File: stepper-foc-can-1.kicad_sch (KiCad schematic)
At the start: 0 parts

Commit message: schem: add stm32g474
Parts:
- added U1: STM32G474RBTx, Package_QFP:LQFP-64_10x10mm_P0.5mm, symbol MCU_ST_STM32G4:STM32G474RBTx
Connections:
- new net GND: U1.15 (VSS), U1.27 (VSSA), U1.31 (VSS), U1.47 (VSS), U1.63 (VSS)

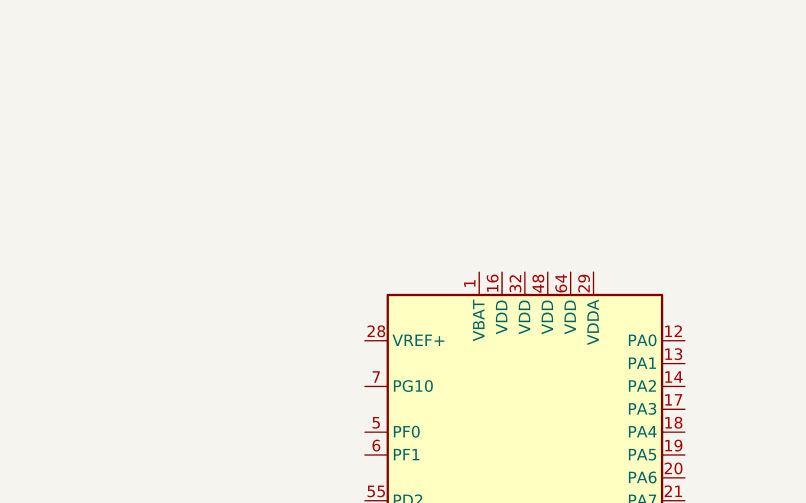
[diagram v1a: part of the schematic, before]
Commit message: schem: add stm32 decoupling caps
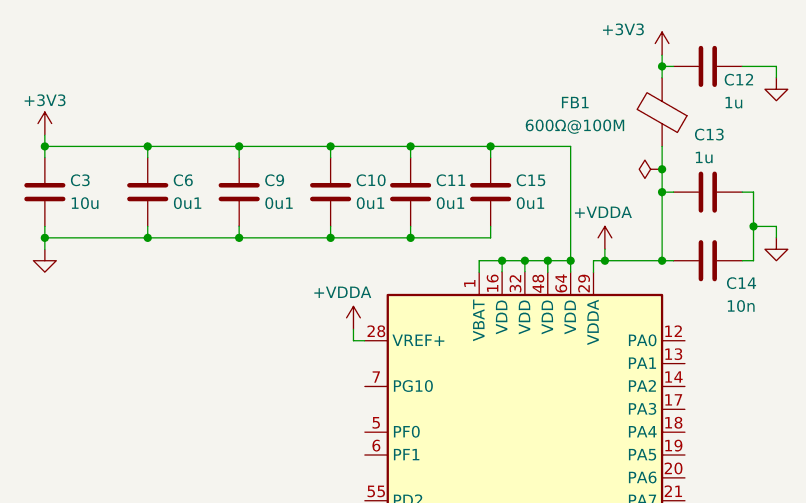
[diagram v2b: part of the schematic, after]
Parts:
- added C10, C11, C15, C6, C9: 0u1, Capacitor_SMD:C_0402_1005Metric, symbol Device:C
- added C12, C13: 1u, Capacitor_SMD:C_0402_1005Metric, symbol Device:C
- added C14: 10n, Capacitor_SMD:C_0402_1005Metric, symbol Device:C
- added C3: 10u, Capacitor_SMD:C_0805_2012Metric, symbol Device:C
- added FB1: 600Ω@100M, Inductor_SMD:L_0805_2012Metric, symbol Device:FerriteBead
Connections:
- net GND: now also C10.2, C11.2, C12.2, C13.2, C14.2, C15.2, C3.2, C6.2, C9.2
- net +3V3: now reaches U1.1 (VBAT)
- net +3V3: now also U1.16 (VDD), U1.32 (VDD), U1.48 (VDD), U1.64 (VDD), C10.1, C11.1, C12.1, C15.1, C3.1, C6.1, C9.1, FB1.2
- net +VDDA: now reaches U1.28 (VREF+)
- net +VDDA: now also U1.29 (VDDA), C13.1, C14.1, FB1.1

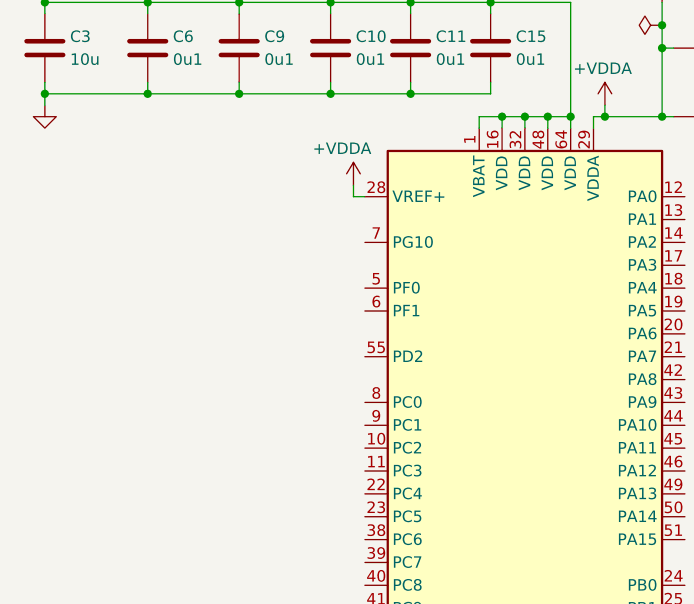
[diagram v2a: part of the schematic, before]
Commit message: schem: add hse and reset
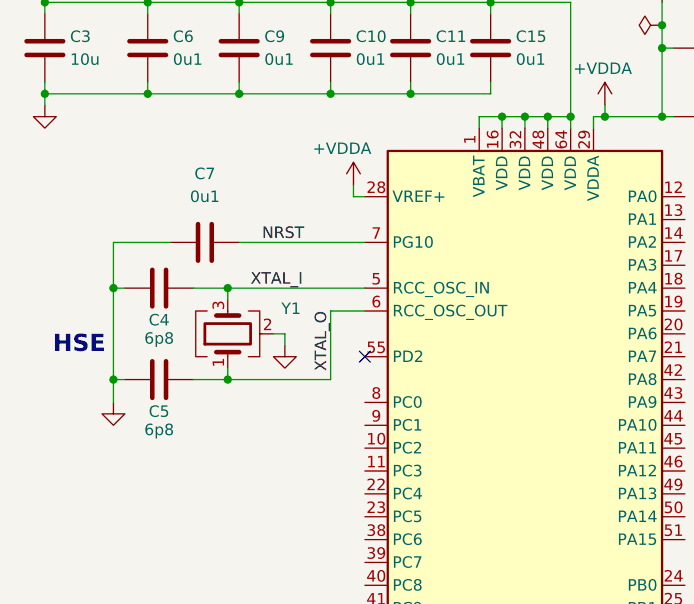
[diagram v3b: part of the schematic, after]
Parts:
- added C4, C5: 6p8, Capacitor_SMD:C_0603_1608Metric, symbol Device:C
- added C7: 0u1, Capacitor_SMD:C_0402_1005Metric, symbol Device:C
- added Y1: Crystal_GND24, Crystal:Crystal_SMD_2016-4Pin_2.0x1.6mm, symbol Device:Crystal_GND24
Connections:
- net GND: now also C4.2, C5.2, C7.1, Y1.2 (G), Y1.4 (G)
- net XTAL_I: now reaches U1.5 (PF0)
- net XTAL_I: now also C4.1, Y1.3
- net XTAL_O: now reaches U1.6 (PF1)
- net XTAL_O: now also C5.1, Y1.1
- net NRST: now reaches U1.7 (PG10)
- net NRST: now also C7.2
- no-connect marks 0 -> 1
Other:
- note added: "HSE"

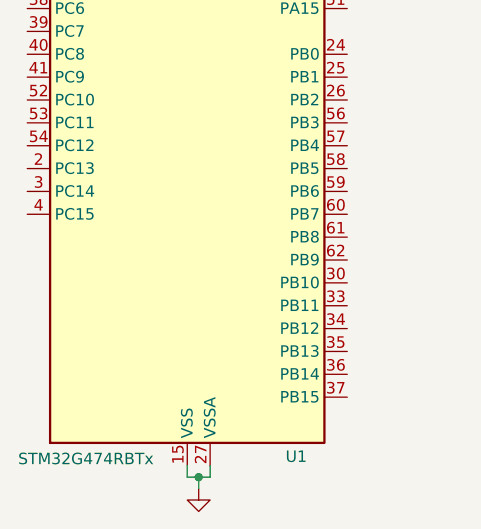
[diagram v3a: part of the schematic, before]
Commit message: schem: add boot
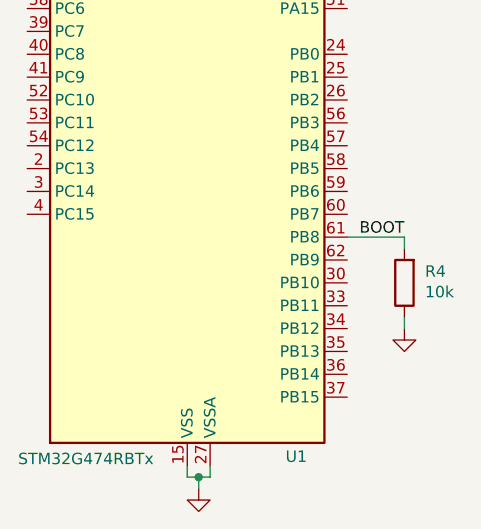
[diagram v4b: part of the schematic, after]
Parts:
- added R4: 10k, Resistor_SMD:R_0402_1005Metric, symbol Device:R
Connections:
- net GND: now also R4.1
- net BOOT: now reaches U1.61 (PB8)
- net BOOT: now also R4.2
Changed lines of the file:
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@@
+	(wire
+		(pts
+			(xy 127 127) (xy 127 128.27)
+		)
+		(stroke
+			(width 0)
+			(type default)
+		)
+	)
 	(wire
 		(pts
@@
 	(wire
 		(pts
+			(xy 127 118.11) (xy 120.65 118.11)
+		)
+		(stroke
+			(width 0)
+			(type default)
+		)
+	)
+	(wire
+		(pts
 			(xy 105.41 144.78) (xy 104.14 144.78)
 		)
@@
 		(pts
 			(xy 128.27 38.1) (xy 127 38.1)
+		)
+		(stroke
+			(width 0)
+			(type default)
+		)
+	)
+	(wire
+		(pts
+			(xy 127 118.11) (xy 127 119.38)
 		)
 		(stroke
@@
 			)
 			(justify left bottom)
+		)
+	)
+	(label "BOOT"
+		(at 127 118.11 180)
+		(effects
+			(font
+				(size 1.27 1.27)
+			)
+			(justify right bottom)
 		)
 	)
@@
 	)
 	(symbol
+		(lib_id "power:GND")
+		(at 127 128.27 0)
+		(mirror y)
+		(unit 1)
+		(body_style 1)
+		(exclude_from_sim no)
+		(in_bom yes)
+		(on_board yes)
+		(in_pos_files yes)
+		(dnp no)
+		(fields_autoplaced yes)
+		(property "Reference" "#PWR016"
+			(at 127 134.62 0)
+			(hide yes)
+			(show_name no)
+			(do_not_autoplace no)
+			(effects
+				(font
+					(size 1.27 1.27)
+				)
+			)
+		)
+		(property "Value" "GND"
+			(at 127 133.35 0)
+			(hide yes)
+			(show_name no)
+			(do_not_autoplace no)
+			(effects
+				(font
+					(size 1.27 1.27)
+				)
+			)
+		)
+		(property "Footprint" ""
+			(at 127 128.27 0)
+			(hide yes)
+			(show_name no)
+			(do_not_autoplace no)
+			(effects
+				(font
+					(size 1.27 1.27)
+				)
+			)
+		)
+		(property "Datasheet" ""
+			(at 127 128.27 0)
+			(hide yes)
+			(show_name no)
+			(do_not_autoplace no)
+			(effects
+				(font
+					(size 1.27 1.27)
+				)
+			)
+		)
+		(property "Description" "Power symbol creates a global label with name \"GND\" , ground"
+			(at 127 128.27 0)
+			(hide yes)
+			(show_name no)
+			(do_not_autoplace no)
+			(effects
+				(font
+					(size 1.27 1.27)
+				)
+			)
+		)
+		(pin "1"
+		)
+		(instances
+			(project "stepper-foc-can-1"
+				(path "/7e511d2f-8abe-4907-a647-133ba6c8a8df"
+					(reference "#PWR016")
+					(unit 1)
+				)
+			)
+		)
+	)
+	(symbol
 		(lib_id "Device:FerriteBead")
 		(at 118.11 29.21 180)
@@
 					(unit 1)
 				)
+			)
+		)
+	)
+	(symbol
+		(lib_id "Device:R")
+		(at 127 123.19 180)
+		(unit 1)
+		(body_style 1)
+		(exclude_from_sim no)
+		(in_bom yes)
+		(on_board yes)
+		(in_pos_files yes)
+		(dnp no)
+		(property "Reference" "R4"
+			(at 129.286 121.92 0)
+			(show_name no)
+			(do_not_autoplace no)
+			(effects
+				(font
+					(size 1.27 1.27)
+				)
+				(justify right)
+			)
+		)
+		(property "Value" "10k"
+			(at 129.286 124.206 0)
+			(show_name no)
+			(do_not_autoplace no)
+			(effects
+				(font
+					(size 1.27 1.27)
+				)
+				(justify right)
+			)
+		)
+		(property "Footprint" "Resistor_SMD:R_0402_1005Metric"
+			(at 128.778 123.19 90)
+			(hide yes)
+			(show_name no)
+			(do_not_autoplace no)
+			(effects
+				(font
+					(size 1.27 1.27)
+				)
+			)
+		)
+		(property "Datasheet" ""
+			(at 127 123.19 0)
+			(hide yes)
+			(show_name no)
+			(do_not_autoplace no)
+			(effects
+				(font
+					(size 1.27 1.27)
+				)
+			)
+		)
+		(property "Description" "Resistor"
+			(at 127 123.19 0)
+			(hide yes)
+			(show_name no)
+			(do_not_autoplace no)
+			(effects
+				(font
+					(size 1.27 1.27)
+				)
+			)
+		)
+		(property "Basic" "Y"
+			(at 127 123.19 90)
+			(hide yes)
+			(show_name no)
+			(do_not_autoplace no)
+			(effects
+				(font
+					(size 1.27 1.27)
+				)
+			)
+		)
+		(property "JLCPCB Part #" "C25744"
+			(at 127 123.19 90)
+			(hide yes)
+			(show_name no)
+			(do_not_autoplace no)
+			(effects
+				(font
+					(size 1.27 1.27)
+				)
+			)
+		)
+		(property "Manufacturer" "Uniroyal Elec"
+			(at 127 123.19 90)
+			(hide yes)
+			(show_name no)
+			(do_not_autoplace no)
+			(effects
+				(font
+					(size 1.27 1.27)
+				)
+			)
+		)
+		(property "Manufacturer Part Number" "0402WGF1002TCE"
+			(at 127 123.19 90)
+			(hide yes)
+			(show_name no)
+			(do_not_autoplace no)
+			(effects
+				(font
+					(size 1.27 1.27)
+				)
+			)
+		)
+		(pin "2"
+		)
+		(pin "1"
+		)
+		(instances
+			(project "stepper-foc-can-1"
+				(path "/7e511d2f-8abe-4907-a647-133ba6c8a8df"
+					(reference "R4")
+					(unit 1)
+				)

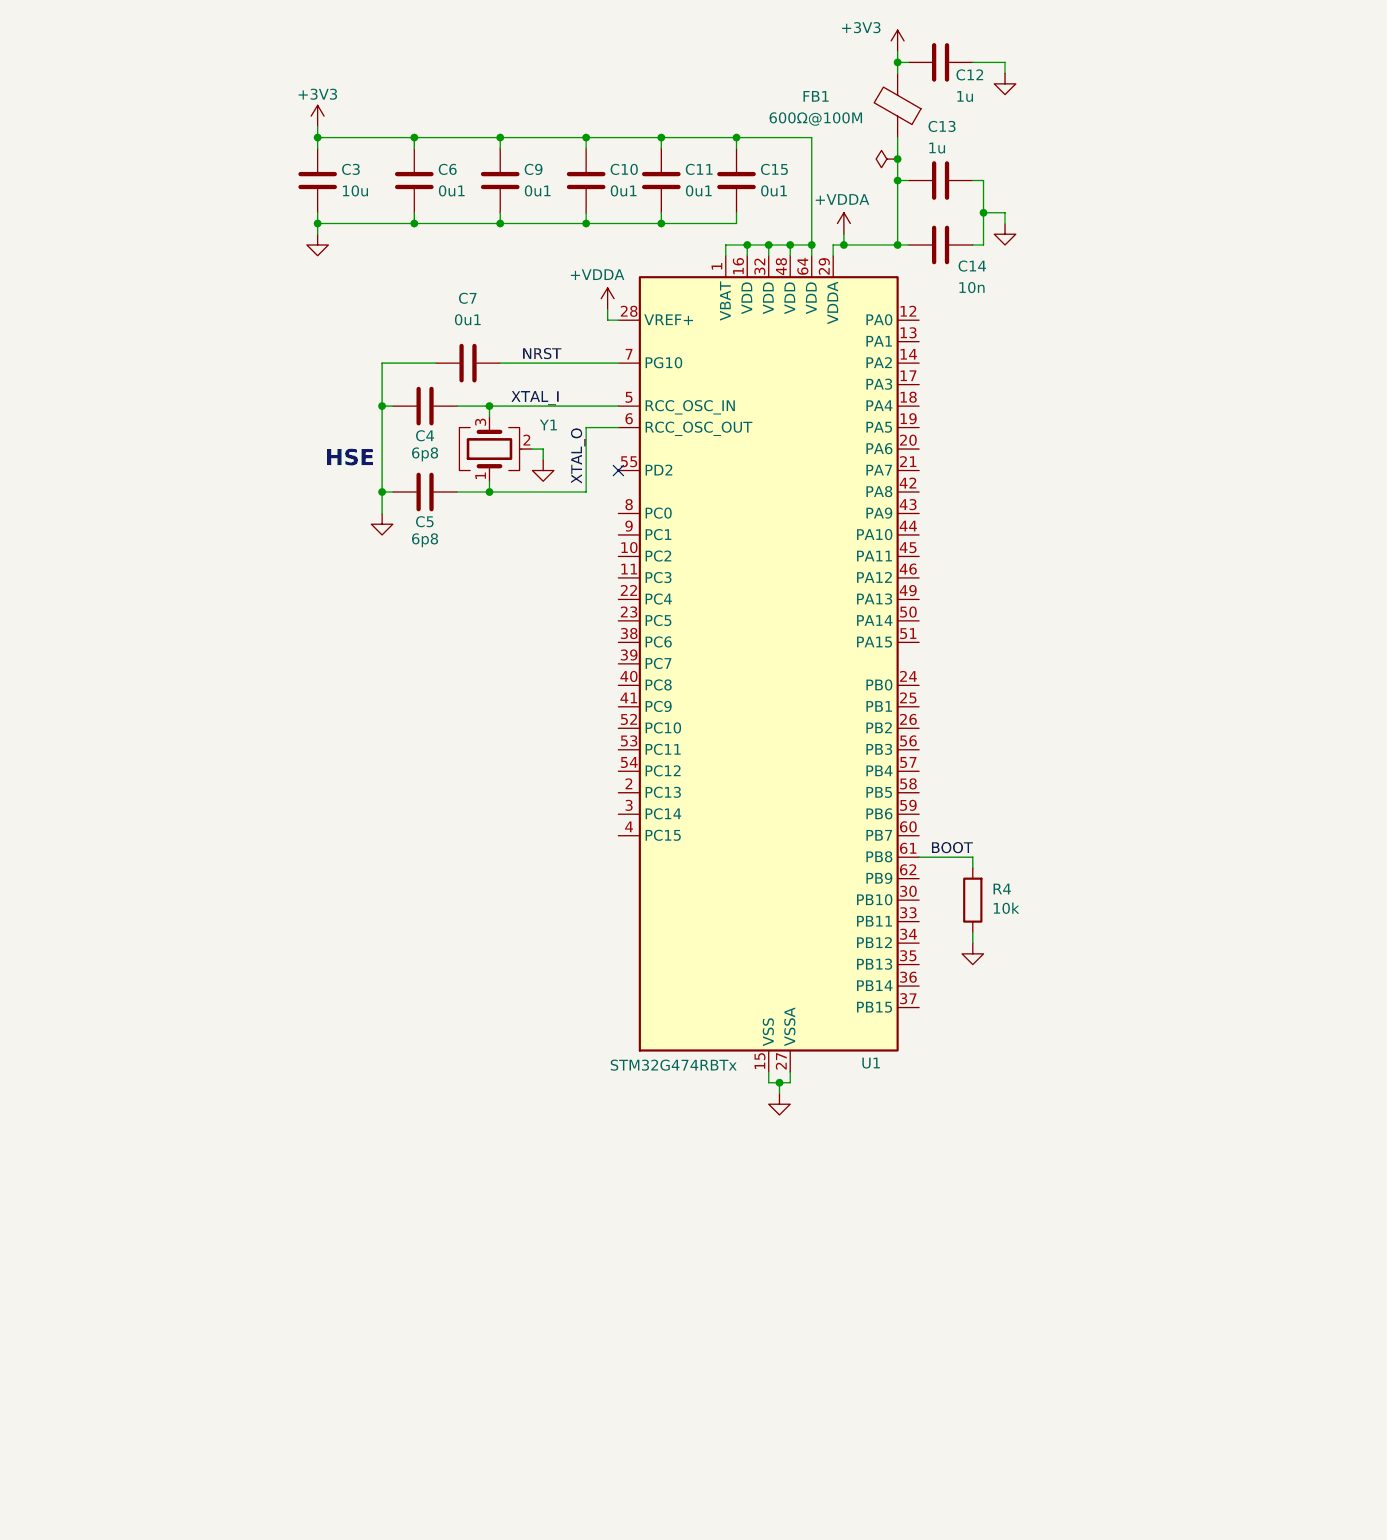
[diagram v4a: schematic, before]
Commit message: schem: add tc2030 swd connector
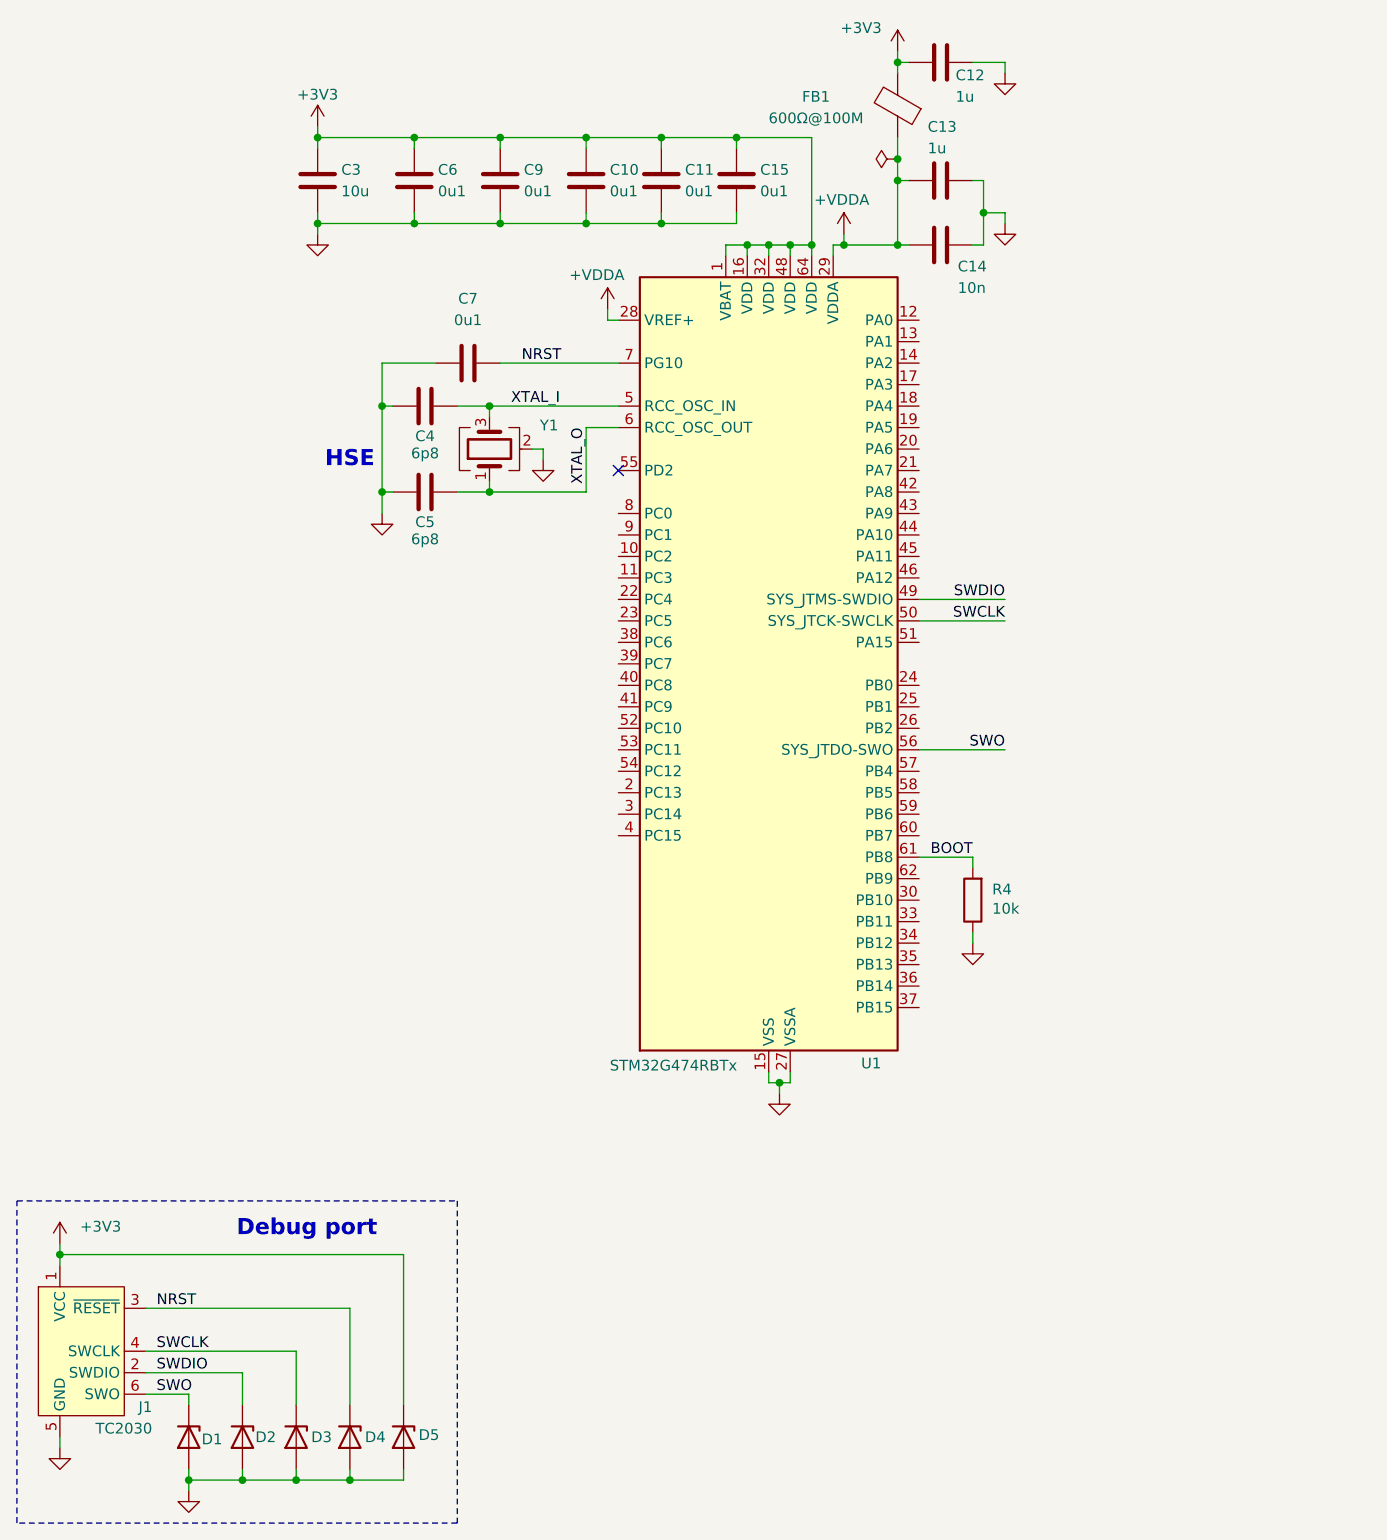
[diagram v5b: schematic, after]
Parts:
- added D1, D2, D3, D4, D5: H5VU10U, GLCS:Diode_DFN1006, symbol GLCS:H5VU10U
- added J1: TC2030, Connector:Tag-Connect_TC2030-IDC-NL_2x03_P1.27mm_Vertical, symbol Connector:Conn_ARM_SWD_TagConnect_TC2030-NL
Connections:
- net +3V3: now also D5.1 (K), J1.1 (VCC)
- net GND: now also D1.2 (A), D2.2 (A), D3.2 (A), D4.2 (A), D5.2 (A), J1.5 (GND)
- net NRST: now also D4.1 (K), J1.3 (~{RESET})
- net SWDIO: now reaches U1.49 (PA13)
- net SWDIO: now also D2.1 (K), J1.2 (SWDIO)
- net SWCLK: now reaches U1.50 (PA14)
- net SWCLK: now also D3.1 (K), J1.4 (SWCLK)
- net SWO: now reaches U1.56 (PB3)
- net SWO: now also D1.1 (K), J1.6 (SWO)
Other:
- note added: "Debug port"

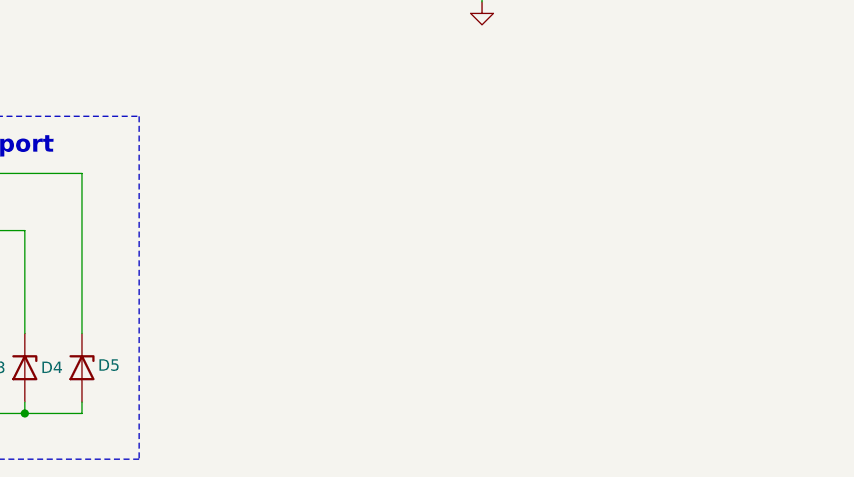
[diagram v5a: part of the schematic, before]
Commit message: schem: add MX25947 5A efuse
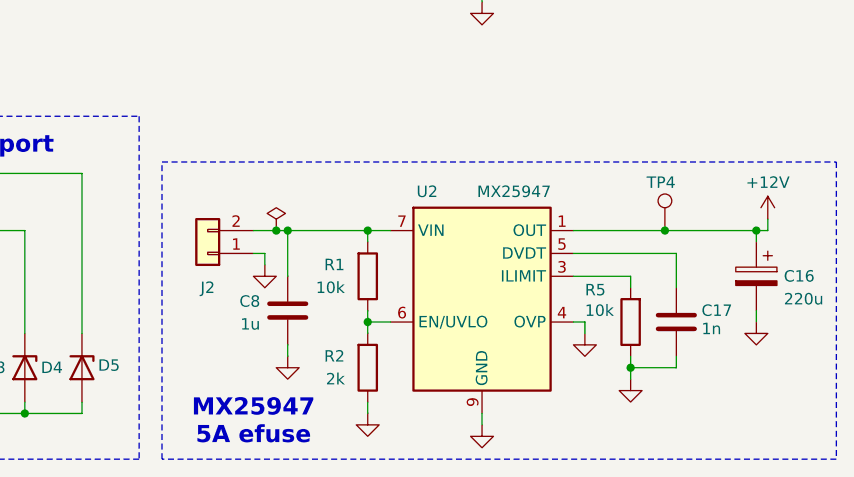
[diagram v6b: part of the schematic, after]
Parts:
- added C16: 220u, Capacitor_SMD:CP_Elec_6.3x7.7, symbol Device:C_Polarized
- added C17: 1n, Capacitor_SMD:C_0402_1005Metric, symbol Device:C
- added C8: 1u, Capacitor_SMD:C_0402_1005Metric, symbol Device:C
- added J2: Conn_01x02, Connector_JST:JST_XH_B2B-XH-A_1x02_P2.50mm_Vertical, symbol Connector_Generic:Conn_01x02
- added R1, R5: 10k, Resistor_SMD:R_0402_1005Metric, symbol Device:R
- added R2: 2k, Resistor_SMD:R_0402_1005Metric, symbol Device:R
- added TP4: TestPoint, TestPoint:TestPoint_Pad_D2.0mm, symbol Connector:TestPoint
- added U2: MX25947, Package_SO:TI_SO-PowerPAD-8_ThermalVias, symbol GLCS:MX25947
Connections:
- net GND: now also C16.2, C17.2, C8.1, J2.1 (Pin_1), R2.1, R5.1, U2.4 (OVP), U2.9 (GND)
- new net: R1.1, R2.2, U2.6 (EN/UVLO)
- new net: R5.2, U2.3 (ILIMIT)
- new net: C17.1, U2.5 (DVDT)
- new net +12V: C16.1, TP4.1, U2.1 (OUT), U2.2 (OUT)
- new net VIN: C8.2, J2.2 (Pin_2), R1.2, U2.7 (VIN), U2.8 (VIN)
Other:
- note added: "MX25947 5A efuse"
